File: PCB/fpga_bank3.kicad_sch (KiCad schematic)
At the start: 12 parts, among them U2 XC7A50T-FGG484

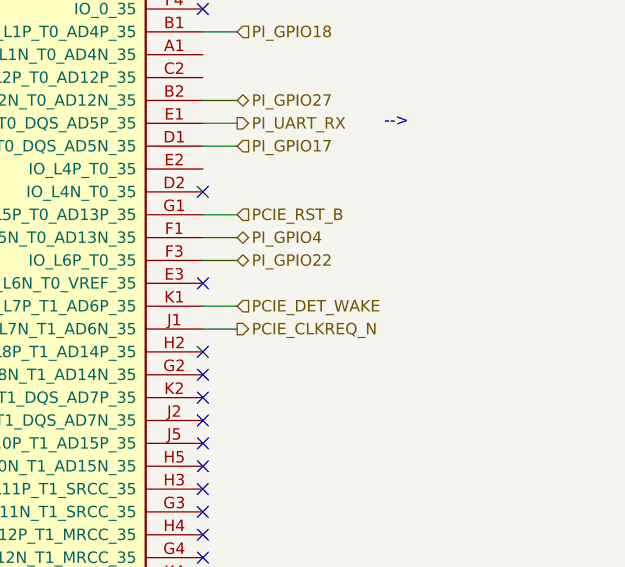
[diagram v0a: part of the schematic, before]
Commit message: Updated PCB to remove MOSI-MISO cross. Updated texts. New images.
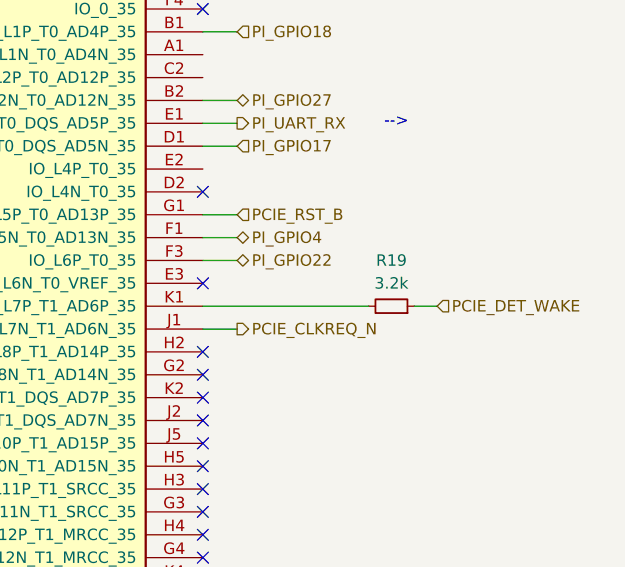
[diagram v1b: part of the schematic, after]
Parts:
- added R19: 3.2k, Resistor_SMD:R_0402_1005Metric, symbol Device:R_Small
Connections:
- net PCIE_DET_WAKE: now also R19.1; no longer U2.K1 (IO_L7P_T1_AD6P_35)
- new net: R19.2, U2.K1 (IO_L7P_T1_AD6P_35)
